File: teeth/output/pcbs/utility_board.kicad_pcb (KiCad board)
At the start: 2 copper layers, 100 x 100 mm, 35 parts

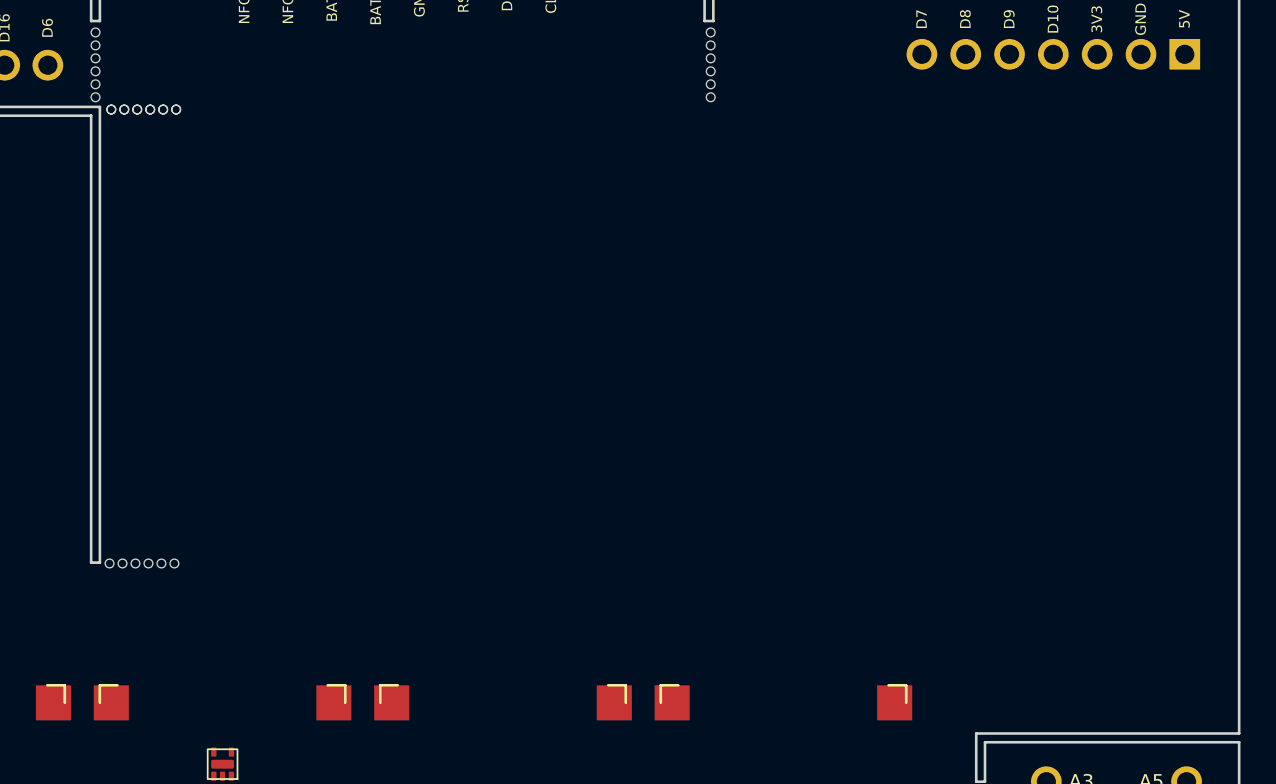
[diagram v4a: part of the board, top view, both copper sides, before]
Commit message: Add more slots/bites to utility board, work on bav70.
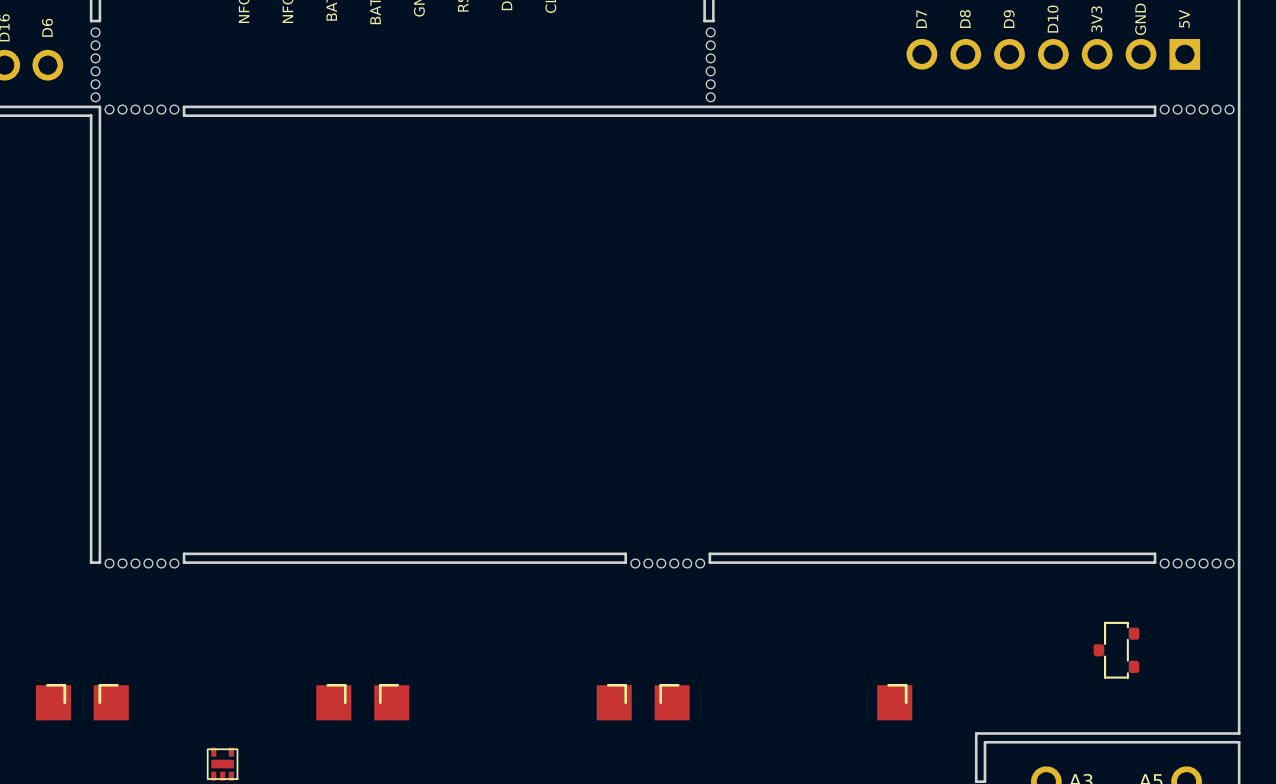
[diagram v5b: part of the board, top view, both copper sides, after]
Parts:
- added D6: , D_MMBD4148PLM, F.Cu at (142.0, 171.5)
- added XX14: , 5diode_Breakout_Holes, F.Cu at (193.0, 185.0)
- added XX15: , 5diode_Breakout_Holes, F.Cu at (193.0, 175.0)
- D4: footprint D_MMBD4148PLM -> SOT-23
- XX11, XX12: value (none) -> mousebites 2mm; footprint 5diode_Breakout_Holes -> mousebites_25mm
- moved XX7 65.4 mm to (197.6, 160.0)
- moved D4 55.7 mm to (193.0, 165.0), turned to 90 degrees
- moved XX12 51.1 mm to (197.6, 134.1)
- moved XX11 43.4 mm to (167.4, 160.0)
- moved XX13 20.0 mm to (193.0, 195.0)
- moved D5 16.0 mm to (142.0, 187.5)
- moved XX6 0.10 mm to (137.4, 134.1)
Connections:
- D4 pad 1: index_home -> 5A1
- D4 pad 2: middle_home -> 5A2
- D4 pad 3: ring_home -> 5C1
- D5 pad 1: index_top -> index_home
- D5 pad 2: middle_top -> middle_home
- D5 pad 3: ring_top -> ring_home
- D5 pad 4: inner_top -> inner_home
- D5 pad 5: pinky_top -> pinky_home
- D5 pad 6: P1.03 -> P0.03
- XX13 pad 1: 3A1 -> 1A1
- XX13 pad 2: 3A2 -> 1A2
- XX13 pad 3: 3A3 -> 1A3
- XX13 pad 4: 3A4 -> 1A4
- XX13 pad 5: 3A5 -> 1A5
- XX13 pad 6: 3C1 -> 1C1
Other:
- outline, holes or cut-outs redrawn

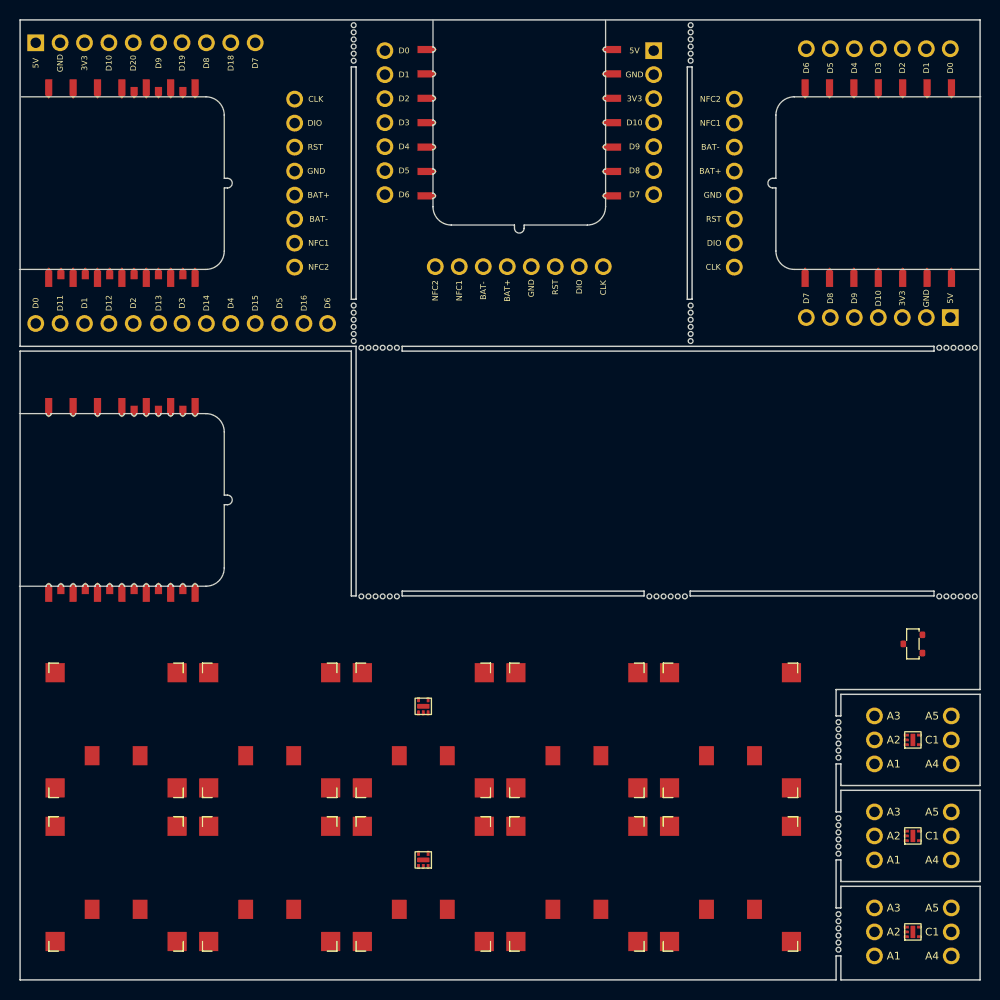
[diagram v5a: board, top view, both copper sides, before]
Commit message: Add BAV70 breakouts and associated slots/bites.
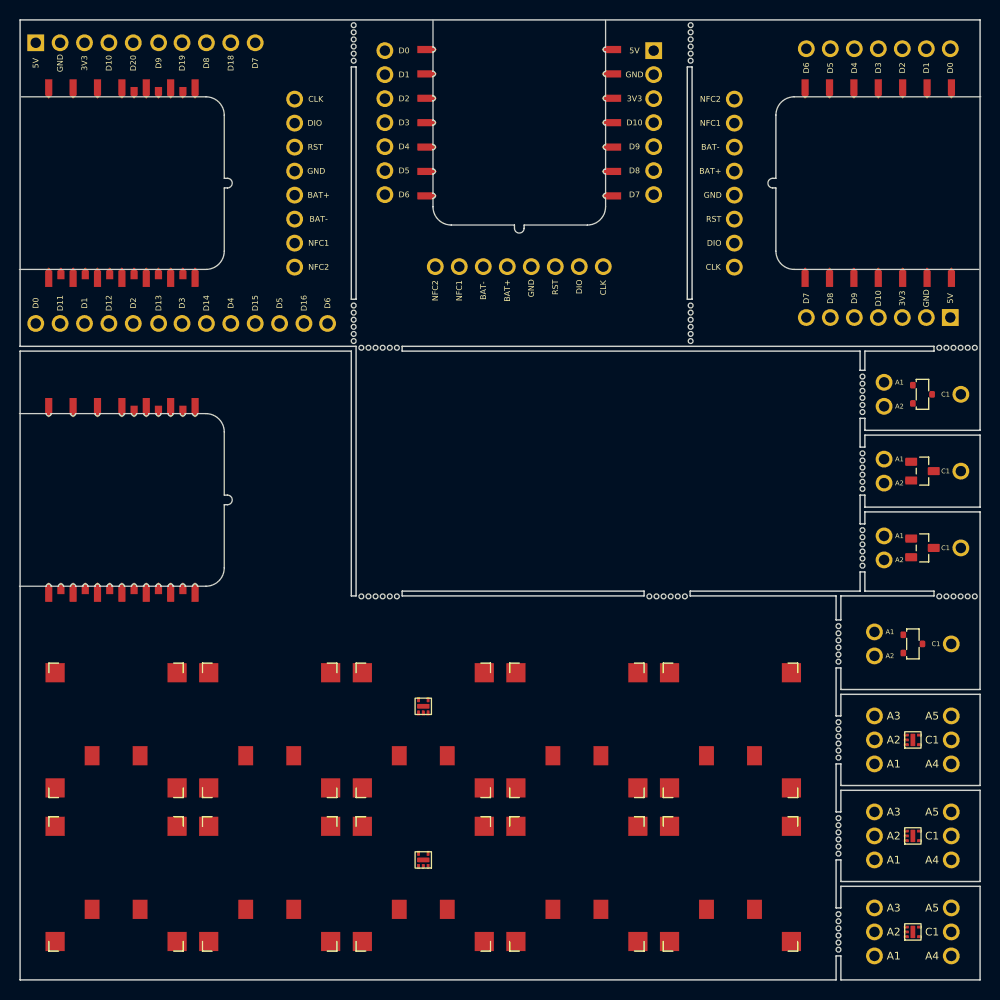
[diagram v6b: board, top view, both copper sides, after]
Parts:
- added D7: , SOT-23, F.Cu at (194.0, 139.0)
- added D8: , D_MMBD4148PLM, F.Cu at (142.0, 187.5)
- added D9: , D_MMBD4148PLM, F.Cu at (142.0, 171.5)
- added XX16: mousebites 2mm, mousebites_25mm, F.Cu at (187.8, 155.0)
- added XX17: , 5diode_Breakout_Holes, F.Cu at (193.0, 195.0)
- added XX18: , 5diode_Breakout_Holes, F.Cu at (193.0, 185.0)
- added XX19: , 5diode_Breakout_Holes, F.Cu at (193.0, 175.0)
- added XX20: , 5diode_Breakout_Holes, F.Cu at (194.0, 155.0)
- added XX21: , 5diode_Breakout_Holes, F.Cu at (193.0, 165.0)
- added XX22: , 5diode_Breakout_Holes, F.Cu at (194.0, 147.0)
- added XX23: , 5diode_Breakout_Holes, F.Cu at (194.0, 139.0)
- D4: value (none) -> BAV70; footprint SOT-23 -> BAV70 SOT23
- D5: footprint D_MMBD4148PLM -> SOT-23
- D6: value (none) -> BAV70; footprint D_MMBD4148PLM -> BAV70 SOT23
- XX13, XX14, XX15: value (none) -> mousebites 2mm; footprint 5diode_Breakout_Holes -> mousebites_25mm
- moved D6 57.5 mm to (194.0, 147.0), turned to -90 degrees
- moved D5 55.7 mm to (193.0, 165.0), turned to -90 degrees
- moved XX14 38.4 mm to (187.8, 147.0), turned to 0 degrees
- moved XX15 36.4 mm to (187.8, 139.0), turned to 0 degrees
- moved XX13 31.0 mm to (185.3, 165.0), turned to 0 degrees
- moved D4 10.0 mm to (194.0, 155.0), turned to -90 degrees
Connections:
- D4 pad 1: 5A1 -> 4A1
- D4 pad 2: 5A2 -> 4A2
- D4 pad 3: 5C1 -> 4C1
- D5 pad 1: index_home -> 5A1
- D5 pad 2: middle_home -> 5A2
- D5 pad 3: ring_home -> 5C1
- D6 pad 1: index_top -> 6A1
- D6 pad 2: middle_top -> 6A2
- D6 pad 3: ring_top -> 6C1
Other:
- outline, holes or cut-outs redrawn

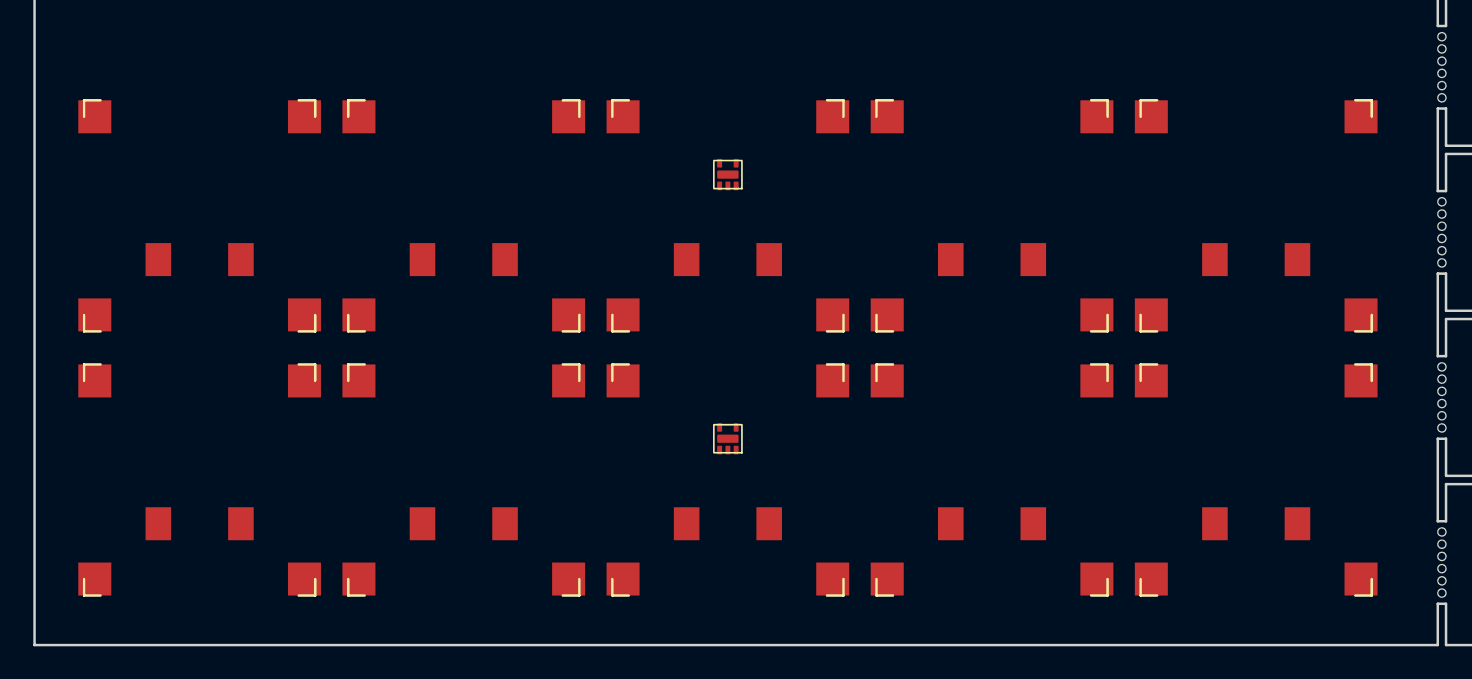
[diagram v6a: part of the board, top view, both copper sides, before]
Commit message: Fix PG1316S footprint (add stabilizer holes)
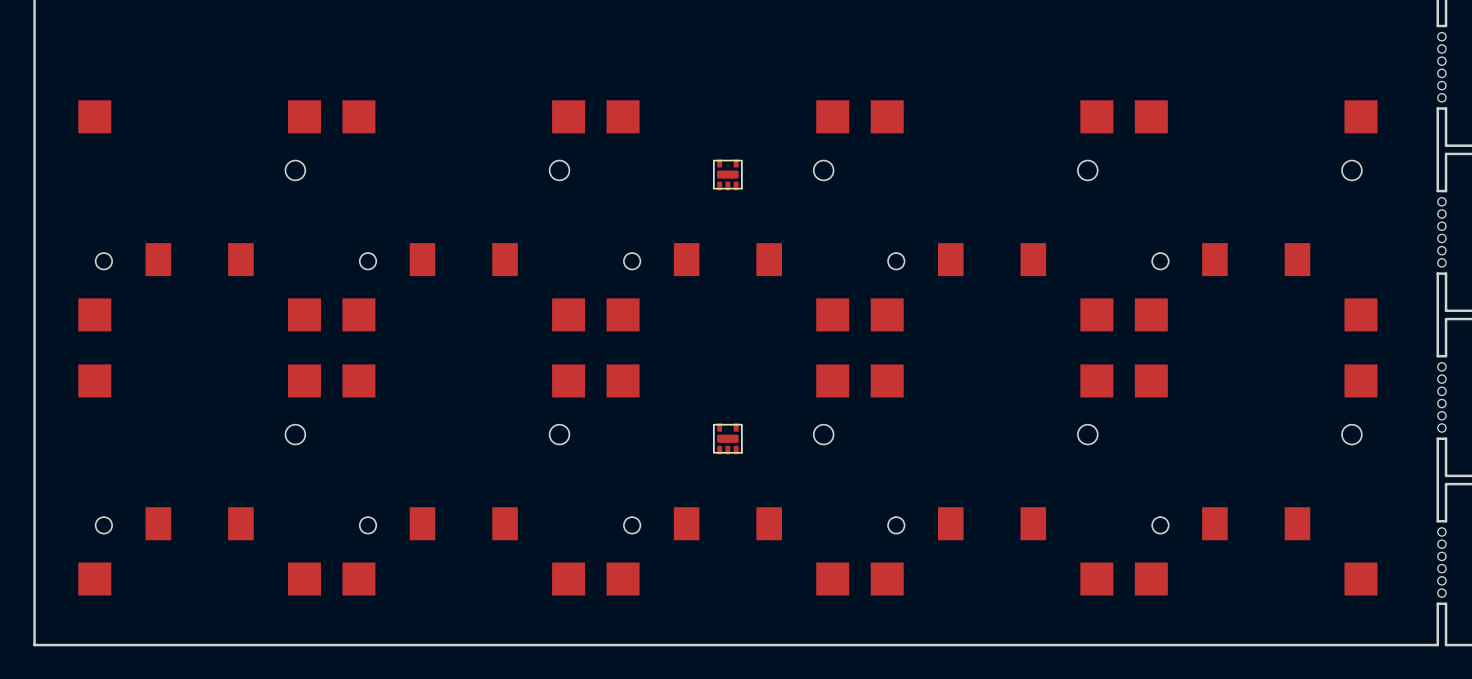
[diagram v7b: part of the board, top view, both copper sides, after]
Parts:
- S1, S10, S2, S3, S4, S5, S6, S7, S8, S9: footprint PG1316S -> CPG1316S01D02_mikeholscher
